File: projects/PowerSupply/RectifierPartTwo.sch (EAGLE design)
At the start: 12 parts, among them K2 G2R2, X1 LINE-IN, X5 T2-PRI, X6 T2-SEC, X7 R2-OUT

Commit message: feat: rectifier part two modified
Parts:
- removed C5, C6: 2200µF, rcl:CPOL-EUE7.5-16
- removed D3: B40C5000-3300A, bb84:B40C5000-3300A
- removed F5: 6.3AT, fuse:SH22,5A
- removed X6: T2-SEC, con-wago-508:W237-04P
- removed X7: R2-OUT, con-wago-508:W237-05P
- added C1, C2: 2200µF, rcl:CPOL-EUE7.5-16
- added D1: B40C5000-3300A, bb84:B40C5000-3300A
- added F2, F3: 6.3AT, fuse:SH22,5A
- added X3: T2-SEC, con-wago-508:W237-06P
- added X4: R2-OUT, con-wago-508:W237-03P
- renumbered F4 to F1, K2 to K1, RX2 to RX1, V2 to V1, X5 to X2
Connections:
- removed net N$12: D3.VAC2, X6-2.KL, X7-1.KL
- removed net N$17: F5.1, X6-1.KL, X7-2.KL
- removed net N$18: D3.VAC1, F5.2
- removed net N$22: C5.-, C6.+, X6-3.KL, X6-4.KL, X7-4.KL
- new net GND: C1.-, C2.+, X3-5.KL, X3-6.KL, X4-2.KL
- new net N$2: D1.VAC2, X3-2.KL, X3-4.KL
- new net N$3: F2.1, F3.2, X3-1.KL
- new net N$5: D1.VAC1, F2.2
- new net N$6: F3.1, X3-3.KL
- net N$20: now also C1.+, D1.+VDC, X4-3.KL; no longer C5.+, D3.+VDC, X7-3.KL
- net N$21: now also C2.-, D1.-VDC, X4-1.KL; no longer C6.-, D3.-VDC, X7-5.KL

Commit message: feat: rectifier part two modified
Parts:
- C2: value 2200µF -> 4700µF
- F2: value 6.3AT -> 4A
- X4: value R2-OUT -> (none); device con-wago-508:W237-03P -> con-wago-508:W237-02P
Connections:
- removed net GND: C1.-, C2.+, X3-5.KL, X3-6.KL, X4-2.KL
- removed net N$20: C1.+, D1.+VDC, X4-3.KL
- removed net N$21: C2.-, D1.-VDC, X4-1.KL
- new net N$1: D1.VAC2, X3-2.KL
- new net N$4: F3.1, X3-6.KL
- net N$2: now also D1.VAC1, F3.2, X3-1.KL; no longer D1.VAC2, X3-2.KL, X3-4.KL
- net N$3: now also D1.+VDC; no longer F3.2, X3-1.KL
- net N$5: now also C1.+, C2.+, X4-2.KL; no longer D1.VAC1
- net N$6: now also C1.-, C2.-, D1.-VDC, X4-1.KL; no longer F3.1, X3-3.KL
- net PE: now also X3-3.KL, X3-4.KL, X3-5.KL
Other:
- moved on the sheet: C1, C2, D1, F2, F3, X2-1, X2-2, X2-3, X2-4, X4-1, X4-2

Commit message: feat: rectifier parts modified
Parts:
- F1: value 1.6AT -> 1AT
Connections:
- new net N$7: X3-3.KL, X3-4.KL
- net N$1: now also F3.2, X3-6.KL; no longer X3-2.KL
- net N$2: now also X3-2.KL; no longer F3.2
- net N$4: now also X3-5.KL; no longer X3-6.KL
- net PE: no longer X3-3.KL, X3-4.KL, X3-5.KL
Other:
- moved on the sheet: F3, X2-1, X2-2, X2-3, X2-4
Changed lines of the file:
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@@
 <part name="FRAME1" library="frames" library_urn="urn:adsk.eagle:library:229" deviceset="A4L-LOC" device=""/>
 <part name="V1" library="varistor" library_urn="urn:adsk.eagle:library:410" deviceset="S20K230" device="" package3d_urn="urn:adsk.eagle:package:30579/1"/>
-<part name="F1" library="fuse" library_urn="urn:adsk.eagle:library:233" deviceset="SH22,5A" device="" package3d_urn="urn:adsk.eagle:package:14070/1" value="1.6AT"/>
+<part name="F1" library="fuse" library_urn="urn:adsk.eagle:library:233" deviceset="SH22,5A" device="" package3d_urn="urn:adsk.eagle:package:14070/1" value="1AT"/>
 <part name="X2" library="con-wago-508" library_urn="urn:adsk.eagle:library:196" deviceset="W237-04P" device="" package3d_urn="urn:adsk.eagle:package:10735/1" value="T2-PRI"/>
 <part name="K1" library="relay" library_urn="urn:adsk.eagle:library:339" deviceset="G2R2" device="" package3d_urn="urn:adsk.eagle:package:24328/1"/>
@@
 <part name="X3" library="con-wago-508" library_urn="urn:adsk.eagle:library:196" deviceset="W237-06P" device="" package3d_urn="urn:adsk.eagle:package:10742/1" value="T2-SEC"/>
 <part name="F3" library="fuse" library_urn="urn:adsk.eagle:library:233" deviceset="SH22,5A" device="" package3d_urn="urn:adsk.eagle:package:14070/1" value="6.3AT"/>
-<part name="PE2" library="supply1" library_urn="urn:adsk.eagle:library:371" deviceset="PE" device=""/>
 <part name="X4" library="con-wago-508" library_urn="urn:adsk.eagle:library:196" deviceset="W237-02P" device="" package3d_urn="urn:adsk.eagle:package:10734/1"/>
 </parts>
@@
 <attribute name="VALUE" x="49.53" y="136.779" size="1.778" layer="96"/>
 </instance>
-<instance part="X2" gate="-1" x="99.06" y="139.7" smashed="yes" rot="MR0">
-<attribute name="NAME" x="100.33" y="140.589" size="1.778" layer="95" rot="MR180"/>
-</instance>
-<instance part="X2" gate="-2" x="99.06" y="119.38" smashed="yes" rot="MR0">
-<attribute name="NAME" x="100.33" y="120.269" size="1.778" layer="95" rot="MR180"/>
-</instance>
-<instance part="X2" gate="-3" x="99.06" y="114.3" smashed="yes" rot="MR0">
-<attribute name="NAME" x="100.33" y="115.189" size="1.778" layer="95" rot="MR180"/>
-</instance>
-<instance part="X2" gate="-4" x="99.06" y="109.22" smashed="yes" rot="MR0">
-<attribute name="VALUE" x="99.06" y="104.14" size="1.778" layer="96"/>
-<attribute name="NAME" x="100.33" y="110.109" size="1.778" layer="95" rot="MR180"/>
+<instance part="X2" gate="-1" x="96.52" y="139.7" smashed="yes" rot="MR0">
+<attribute name="NAME" x="97.79" y="140.589" size="1.778" layer="95" rot="MR180"/>
+</instance>
+<instance part="X2" gate="-2" x="96.52" y="119.38" smashed="yes" rot="MR0">
+<attribute name="NAME" x="97.79" y="120.269" size="1.778" layer="95" rot="MR180"/>
+</instance>
+<instance part="X2" gate="-3" x="96.52" y="114.3" smashed="yes" rot="MR0">
+<attribute name="NAME" x="97.79" y="115.189" size="1.778" layer="95" rot="MR180"/>
+</instance>
+<instance part="X2" gate="-4" x="96.52" y="109.22" smashed="yes" rot="MR0">
+<attribute name="VALUE" x="96.52" y="104.14" size="1.778" layer="96"/>
+<attribute name="NAME" x="97.79" y="110.109" size="1.778" layer="95" rot="MR180"/>
 </instance>
 <instance part="K1" gate="1" x="76.2" y="116.84" smashed="yes">
@@
 <instance part="RX1" gate="G$1" x="81.28" y="139.7" smashed="yes" rot="R90">
 <attribute name="NAME" x="84.0994" y="141.732" size="1.778" layer="95"/>
-<attribute name="VALUE" x="73.787" y="136.652" size="1.778" layer="96"/>
+<attribute name="VALUE" x="73.787" y="144.272" size="1.778" layer="96"/>
 </instance>
 <instance part="X3" gate="-1" x="116.84" y="96.52" smashed="yes">
@@
 <attribute name="NAME" x="115.57" y="72.009" size="1.778" layer="95" rot="R180"/>
 </instance>
-<instance part="F3" gate="1" x="129.54" y="71.12" smashed="yes">
-<attribute name="NAME" x="125.73" y="72.517" size="1.778" layer="95"/>
-<attribute name="VALUE" x="125.73" y="68.199" size="1.778" layer="96"/>
-</instance>
-<instance part="PE2" gate="M" x="142.24" y="76.2" smashed="yes">
-<attribute name="VALUE" x="142.24" y="73.66" size="1.778" layer="96" rot="R180"/>
+<instance part="F3" gate="1" x="129.54" y="76.2" smashed="yes">
+<attribute name="NAME" x="125.73" y="77.597" size="1.778" layer="95"/>
+<attribute name="VALUE" x="125.73" y="73.279" size="1.778" layer="96"/>
 </instance>
 <instance part="X4" gate="-1" x="193.04" y="83.82" smashed="yes" rot="MR0">
@@
 <wire x1="22.86" y1="22.86" x2="20.32" y2="22.86" width="0.1524" layer="91"/>
 </segment>
-<segment>
-<pinref part="PE2" gate="M" pin="PE"/>
-<wire x1="142.24" y1="78.74" x2="142.24" y2="81.28" width="0.1524" layer="91"/>
-<pinref part="X3" gate="-3" pin="KL"/>
-<wire x1="121.92" y1="86.36" x2="124.46" y2="86.36" width="0.1524" layer="91"/>
-<wire x1="124.46" y1="86.36" x2="124.46" y2="81.28" width="0.1524" layer="91"/>
-<pinref part="X3" gate="-4" pin="KL"/>
-<wire x1="124.46" y1="81.28" x2="121.92" y2="81.28" width="0.1524" layer="91"/>
-<pinref part="X3" gate="-5" pin="KL"/>
-<wire x1="121.92" y1="76.2" x2="124.46" y2="76.2" width="0.1524" layer="91"/>
-<wire x1="124.46" y1="76.2" x2="124.46" y2="81.28" width="0.1524" layer="91"/>
-<junction x="124.46" y="81.28"/>
-<wire x1="142.24" y1="81.28" x2="124.46" y2="81.28" width="0.1524" layer="91"/>
-</segment>
 </net>
 <net name="+230VAC" class="0">
@@
 <wire x1="76.2" y1="109.22" x2="63.5" y2="109.22" width="0.1524" layer="91"/>
 <junction x="63.5" y="109.22"/>
-<wire x1="76.2" y1="109.22" x2="93.98" y2="109.22" width="0.1524" layer="91"/>
+<wire x1="76.2" y1="109.22" x2="91.44" y2="109.22" width="0.1524" layer="91"/>
 <junction x="76.2" y="109.22"/>
 <pinref part="X2" gate="-4" pin="KL"/>
@@
 <segment>
 <pinref part="X2" gate="-2" pin="KL"/>
-<wire x1="93.98" y1="119.38" x2="91.44" y2="119.38" width="0.1524" layer="91"/>
-<wire x1="91.44" y1="119.38" x2="91.44" y2="114.3" width="0.1524" layer="91"/>
+<wire x1="91.44" y1="119.38" x2="88.9" y2="119.38" width="0.1524" layer="91"/>
+<wire x1="88.9" y1="119.38" x2="88.9" y2="114.3" width="0.1524" layer="91"/>
 <pinref part="X2" gate="-3" pin="KL"/>
-<wire x1="91.44" y1="114.3" x2="93.98" y2="114.3" width="0.1524" layer="91"/>
+<wire x1="88.9" y1="114.3" x2="91.44" y2="114.3" width="0.1524" layer="91"/>
 </segment>
 </net>
@@
 <pinref part="X2" gate="-1" pin="KL"/>
 <pinref part="RX1" gate="G$1" pin="1"/>
-<wire x1="86.36" y1="139.7" x2="91.44" y2="139.7" width="0.1524" layer="91"/>
-<wire x1="91.44" y1="139.7" x2="93.98" y2="139.7" width="0.1524" layer="91"/>
-<wire x1="91.44" y1="139.7" x2="91.44" y2="124.46" width="0.1524" layer="91"/>
-<junction x="91.44" y="139.7"/>
-<wire x1="91.44" y1="124.46" x2="76.2" y2="124.46" width="0.1524" layer="91"/>
+<wire x1="86.36" y1="139.7" x2="88.9" y2="139.7" width="0.1524" layer="91"/>
+<wire x1="88.9" y1="139.7" x2="91.44" y2="139.7" width="0.1524" layer="91"/>
+<wire x1="88.9" y1="139.7" x2="88.9" y2="124.46" width="0.1524" layer="91"/>
+<junction x="88.9" y="139.7"/>
+<wire x1="88.9" y1="124.46" x2="76.2" y2="124.46" width="0.1524" layer="91"/>
 <pinref part="K1" gate="2" pin="P"/>
 <wire x1="76.2" y1="124.46" x2="76.2" y2="127" width="0.1524" layer="91"/>
@@
 </segment>
 </net>
-<net name="N$1" class="0">
-<segment>
-<pinref part="X3" gate="-2" pin="KL"/>
-<pinref part="D1" gate="G$1" pin="VAC2"/>
-<wire x1="121.92" y1="91.44" x2="142.24" y2="91.44" width="0.1524" layer="91"/>
-</segment>
-</net>
 <net name="N$2" class="0">
 <segment>
 <pinref part="X3" gate="-1" pin="KL"/>
 <pinref part="D1" gate="G$1" pin="VAC1"/>
-<wire x1="121.92" y1="96.52" x2="137.16" y2="96.52" width="0.1524" layer="91"/>
-<pinref part="F3" gate="1" pin="2"/>
-<wire x1="137.16" y1="96.52" x2="142.24" y2="96.52" width="0.1524" layer="91"/>
-<wire x1="134.62" y1="71.12" x2="137.16" y2="71.12" width="0.1524" layer="91"/>
-<wire x1="137.16" y1="71.12" x2="137.16" y2="96.52" width="0.1524" layer="91"/>
-<junction x="137.16" y="96.52"/>
-</segment>
-</net>
-<net name="N$4" class="0">
-<segment>
-<pinref part="X3" gate="-6" pin="KL"/>
-<pinref part="F3" gate="1" pin="1"/>
-<wire x1="121.92" y1="71.12" x2="124.46" y2="71.12" width="0.1524" layer="91"/>
+<wire x1="121.92" y1="96.52" x2="124.46" y2="96.52" width="0.1524" layer="91"/>
+<pinref part="X3" gate="-2" pin="KL"/>
+<wire x1="124.46" y1="96.52" x2="142.24" y2="96.52" width="0.1524" layer="91"/>
+<wire x1="121.92" y1="91.44" x2="124.46" y2="91.44" width="0.1524" layer="91"/>
+<wire x1="124.46" y1="91.44" x2="124.46" y2="96.52" width="0.1524" layer="91"/>
+<junction x="124.46" y="96.52"/>
 </segment>
 </net>
@@
 </segment>
 </net>
+<net name="N$7" class="0">
+<segment>
+<pinref part="X3" gate="-4" pin="KL"/>
+<pinref part="X3" gate="-3" pin="KL"/>
+<wire x1="121.92" y1="86.36" x2="124.46" y2="86.36" width="0.1524" layer="91"/>
+<wire x1="124.46" y1="86.36" x2="124.46" y2="81.28" width="0.1524" layer="91"/>
+<wire x1="124.46" y1="81.28" x2="121.92" y2="81.28" width="0.1524" layer="91"/>
+</segment>
+</net>
+<net name="N$4" class="0">
+<segment>
+<pinref part="X3" gate="-5" pin="KL"/>
+<pinref part="F3" gate="1" pin="1"/>
+<wire x1="121.92" y1="76.2" x2="124.46" y2="76.2" width="0.1524" layer="91"/>
+</segment>
+</net>
+<net name="N$1" class="0">
+<segment>
+<pinref part="X3" gate="-6" pin="KL"/>
+<wire x1="121.92" y1="71.12" x2="137.16" y2="71.12" width="0.1524" layer="91"/>
+<wire x1="137.16" y1="71.12" x2="137.16" y2="76.2" width="0.1524" layer="91"/>
+<pinref part="F3" gate="1" pin="2"/>
+<wire x1="137.16" y1="76.2" x2="134.62" y2="76.2" width="0.1524" layer="91"/>
+<pinref part="D1" gate="G$1" pin="VAC2"/>
+<wire x1="137.16" y1="91.44" x2="142.24" y2="91.44" width="0.1524" layer="91"/>
+<wire x1="137.16" y1="76.2" x2="137.16" y2="91.44" width="0.1524" layer="91"/>
+<junction x="137.16" y="76.2"/>
+</segment>
+</net>

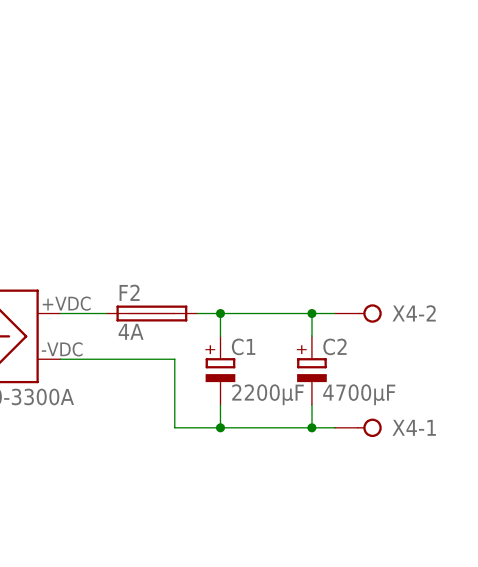
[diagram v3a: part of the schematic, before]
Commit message: feat: rectifier part modified
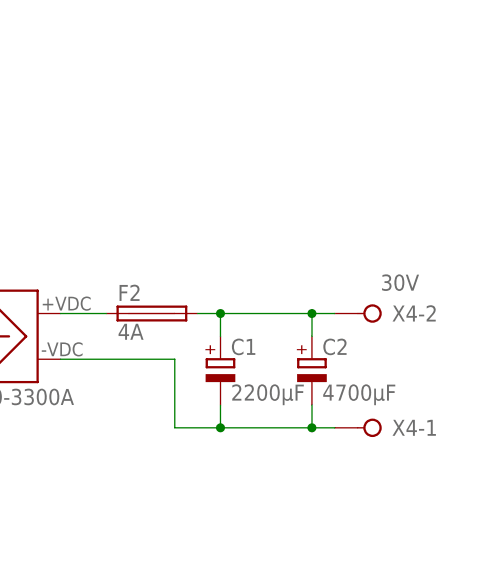
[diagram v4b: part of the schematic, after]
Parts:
- X4: value (none) -> 30V
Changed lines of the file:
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@@
 <part name="X3" library="con-wago-508" library_urn="urn:adsk.eagle:library:196" deviceset="W237-06P" device="" package3d_urn="urn:adsk.eagle:package:10742/1" value="T2-SEC"/>
 <part name="F3" library="fuse" library_urn="urn:adsk.eagle:library:233" deviceset="SH22,5A" device="" package3d_urn="urn:adsk.eagle:package:14070/1" value="6.3AT"/>
-<part name="X4" library="con-wago-508" library_urn="urn:adsk.eagle:library:196" deviceset="W237-02P" device="" package3d_urn="urn:adsk.eagle:package:10734/1"/>
+<part name="X4" library="con-wago-508" library_urn="urn:adsk.eagle:library:196" deviceset="W237-02P" device="" package3d_urn="urn:adsk.eagle:package:10734/1" value="30V"/>
 </parts>
 <sheets>
@@
 </instance>
 <instance part="X4" gate="-2" x="193.04" y="96.52" smashed="yes" rot="MR0">
-<attribute name="VALUE" x="193.04" y="99.06" size="1.778" layer="96" rot="MR0"/>
+<attribute name="VALUE" x="193.04" y="99.06" size="1.778" layer="96"/>
 <attribute name="NAME" x="194.31" y="97.409" size="1.778" layer="95" rot="MR180"/>
 </instance>

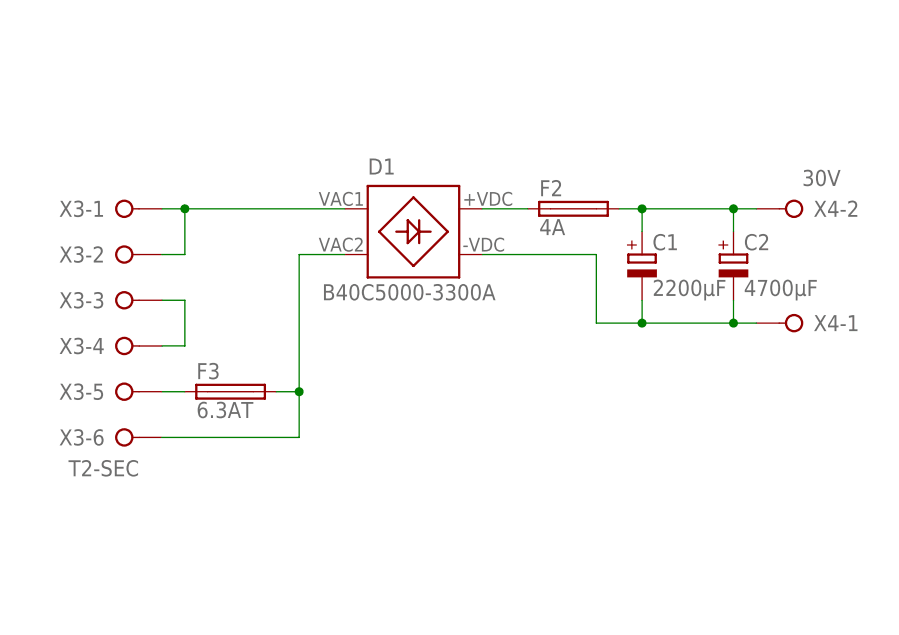
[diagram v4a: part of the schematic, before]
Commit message: feat: rectifier part modified
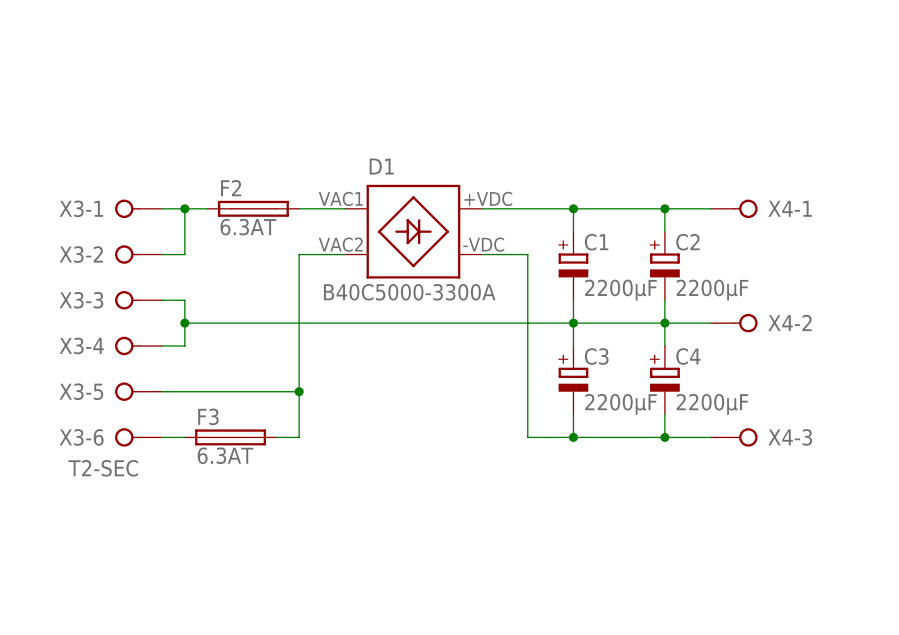
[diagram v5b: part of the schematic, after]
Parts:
- added C3, C4: 2200µF, rcl:CPOL-EUE7.5-16
- C2: value 4700µF -> 2200µF
- F2: value 4A -> 6.3AT
- X4: value 30V -> (none); device con-wago-508:W237-02P -> con-wago-508:W237-03P
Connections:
- removed net N$7: X3-3.KL, X3-4.KL
- new net N$8: D1.VAC1, F2.2
- net N$1: now also X3-5.KL; no longer X3-6.KL
- net N$2: now also F2.1; no longer D1.VAC1
- net N$3: now also C3.-, C4.-, D1.-VDC, X4-3.KL; no longer D1.+VDC, F2.1
- net N$4: now also X3-6.KL; no longer X3-5.KL
- net N$5: now also D1.+VDC, X4-1.KL; no longer F2.2, X4-2.KL
- net N$6: now also C3.+, C4.+, X3-3.KL, X3-4.KL, X4-2.KL; no longer D1.-VDC, X4-1.KL
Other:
- moved on the sheet: C1, C2, F2, F3, X4-1, X4-2
